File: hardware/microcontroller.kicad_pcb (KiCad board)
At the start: 2 copper layers, 50.8 x 78.7 mm, 44 parts, among them J5 1x2 jumper right-angle, J6 Conn_02x03_Odd_Even, J7 1x2 jumper right-angle, U10 74HC670, U11 74HC670, U13 74AHC74, U15 74LVC138, U16 74LV1T125, U17 74LVC138, U18 74LVC2G125, U3 74LV163, U4 74LV163, U5 74LV163, U6 74LV163, U7 74LV163, U8 74LV164, U9 74LV164

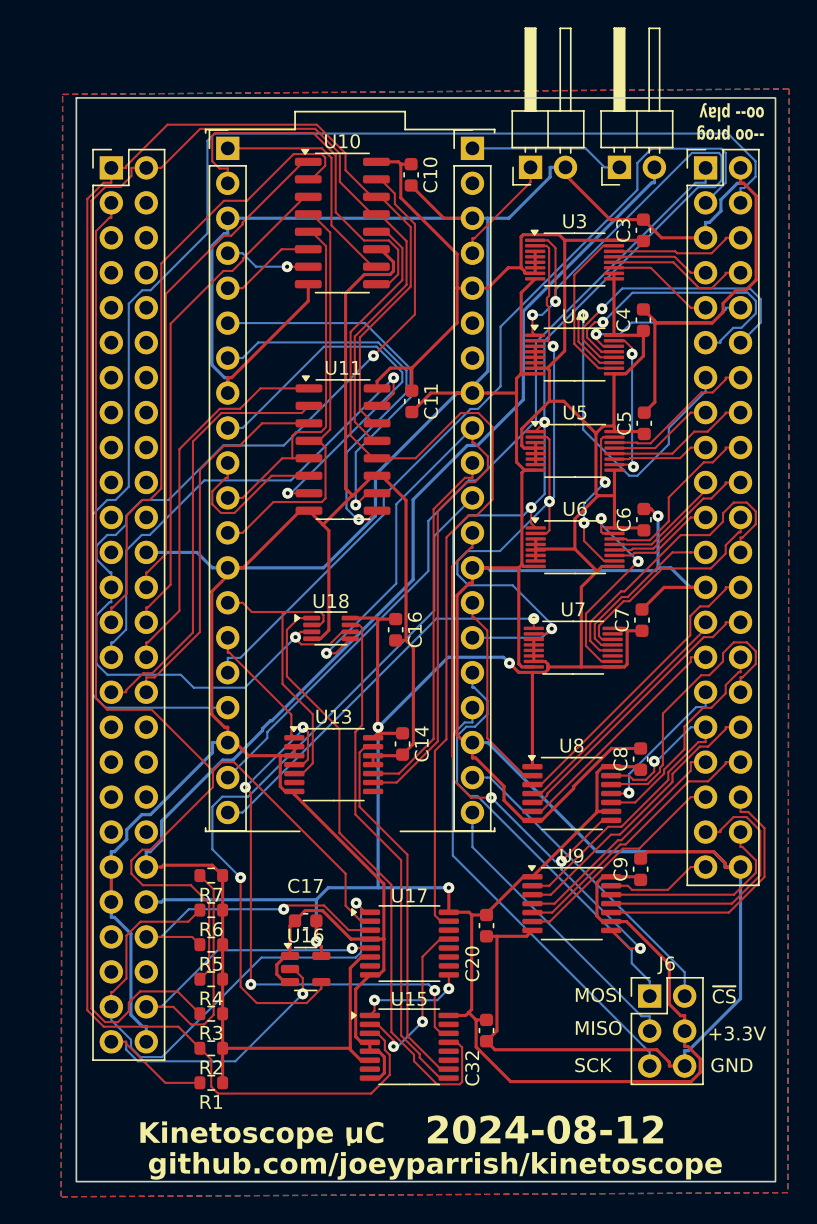
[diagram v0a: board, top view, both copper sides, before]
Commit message: Replace address counters with slightly larger versions that can be assembled more easily
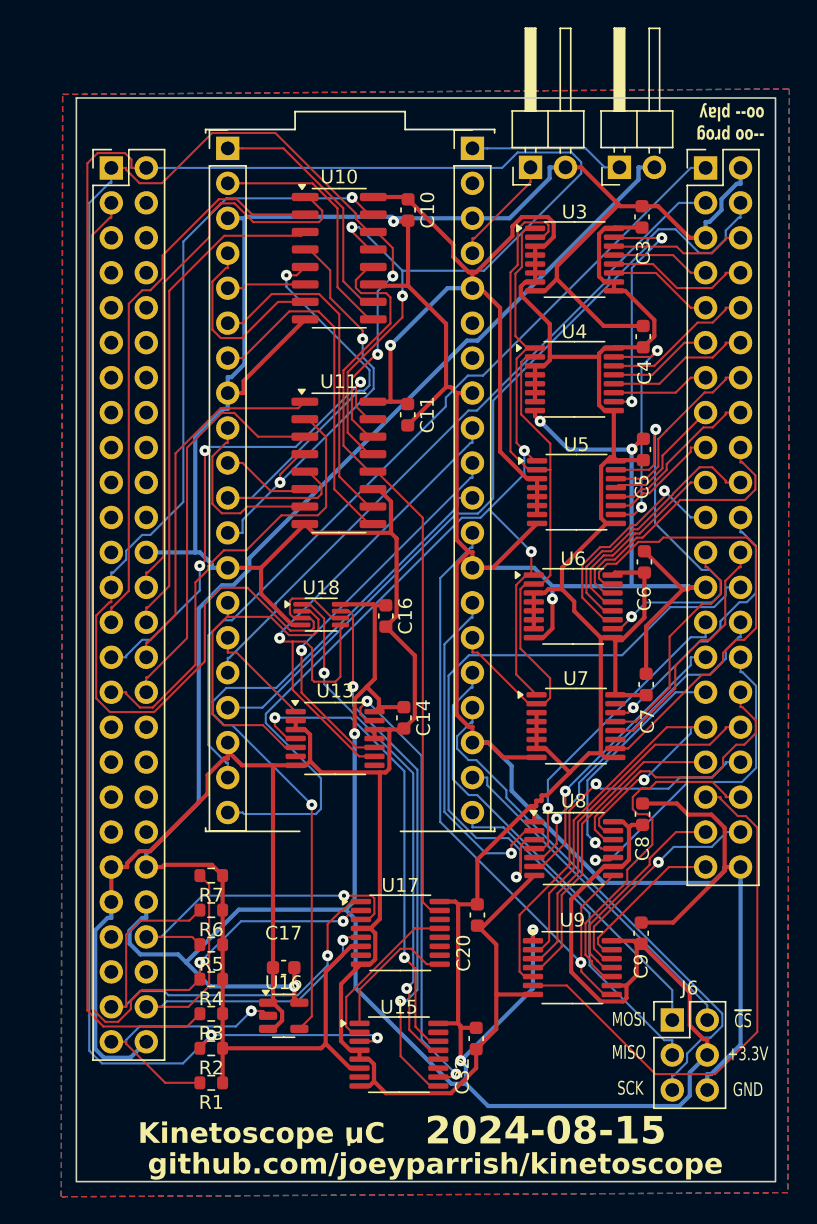
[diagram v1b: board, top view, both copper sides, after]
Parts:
- U3, U4, U5, U6, U7: footprint Package_SO:TSSOP-16_4.4x3.6mm_P0.4mm -> Package_SO:TSSOP-16_4.4x5mm_P0.65mm
- moved U7 5.70 mm to (55.0, 64.9)
- moved C7 4.68 mm to (60.1, 61.9)
- moved C9 4.65 mm to (59.8, 80.0)
- moved U9 4.65 mm to (54.8, 82.5)
- moved U6 4.30 mm to (54.8, 56.2)
- moved C8 4.00 mm to (59.9, 71.3)
- moved U8 4.00 mm to (54.9, 73.8)
- moved C17 3.76 mm to (33.8, 82.5)
- moved U16 3.76 mm to (33.8, 86.0)
- moved C6 3.07 mm to (60.0, 53.0)
- moved U5 3.00 mm to (55.1, 47.9)
- moved C10 2.56 mm to (42.8, 27.4)
- moved U10 2.56 mm to (37.8, 30.9)
- moved J6 2.39 mm to (62.0, 86.3)
- moved C14 1.90 mm to (42.5, 64.3)
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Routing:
- net +3.3V: track 286.7 -> 341.7 mm, vias 4 -> 5
- net /SRAM_DIS_2: track 99.2 -> 59.3 mm
- net GND: track 487.9 -> 451.8 mm, vias 1 -> 4
- net /kinetoscope-header-internal/SEGA_A2: track 115.8 -> 148.4 mm, vias 0 -> 2
- net /data-register-internal/D0: track 22.0 -> 46.1 mm, vias 0 -> 1
- net /data-register-internal/D11: track 16.3 -> 39.8 mm
- net /~{SRAM_W_A_CLR}: track 102.5 -> 79.3 mm, vias 5 -> 2
- net /address-counter-internal/A8: track 28.1 -> 7.12 mm, vias 1 -> 0
- net Net-(U6-TC): track 16.3 -> 34.5 mm, vias 2 -> 0
- net Net-(U5-TC): track 12.0 -> 28.8 mm
- net /REG_R_D6: track 29.8 -> 13.3 mm, vias 1 -> 0
- net /~{REG_WE}: track 69.1 -> 54.6 mm
- net /address-counter-internal/A6: track 22.1 -> 7.64 mm, vias 1 -> 0
- net /SRAM_DIS_1: track 61.4 -> 50.1 mm
- net /address-counter-internal/A7: track 21.9 -> 10.5 mm, vias 1 -> 0
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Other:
- board text added: "2024-08-15"
- board text removed: "2024-08-12"

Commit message: Fix microcontroller address decoders
Verified on a breadboard
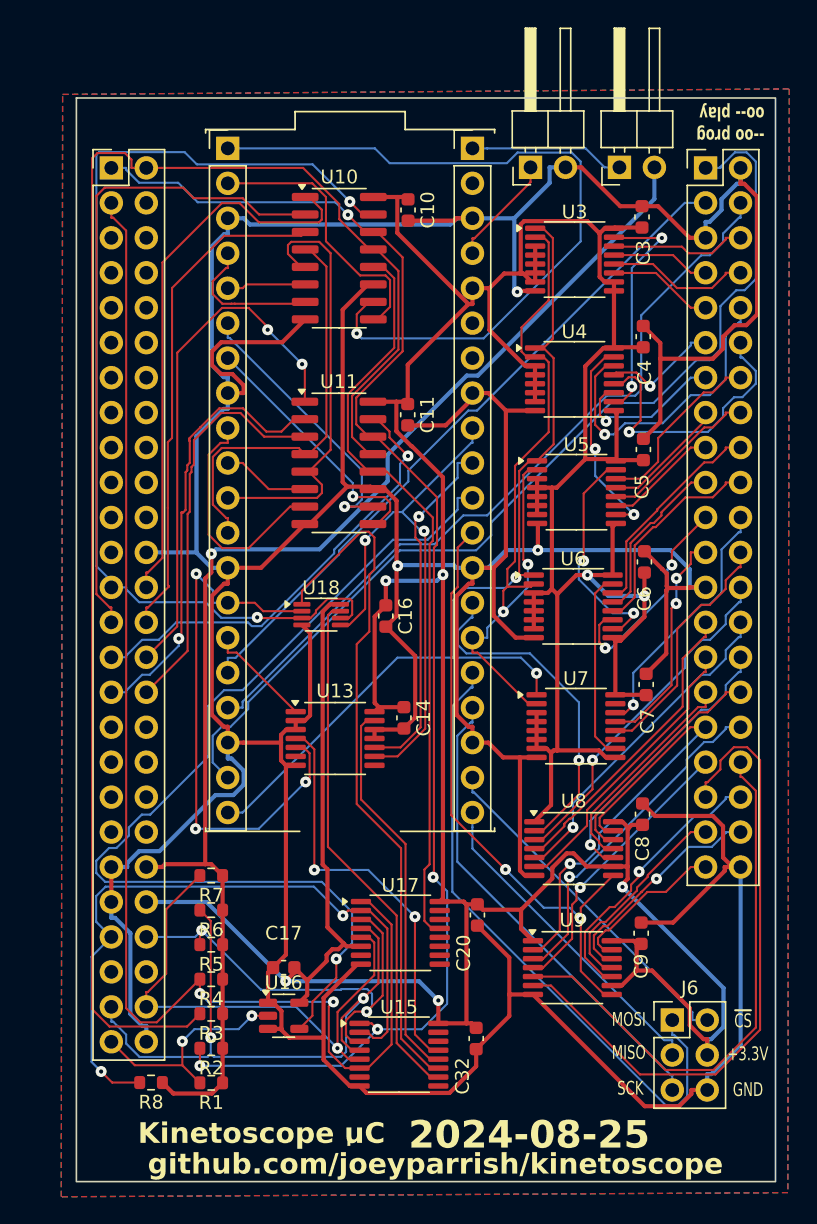
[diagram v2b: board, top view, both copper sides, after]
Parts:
- added R8: 10k, Resistor_SMD:R_0603_1608Metric, F.Cu at (24.2, 90.8)
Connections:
- net /address-counter-internal/A1 renamed /SRAM_W_A0
- net /address-counter-internal/A10 renamed /SRAM_W_A9
- net /address-counter-internal/A11 renamed /SRAM_W_A10
- net /address-counter-internal/A12 renamed /SRAM_W_A11
- net /address-counter-internal/A13 renamed /SRAM_W_A12
- net /address-counter-internal/A14 renamed /SRAM_W_A13
- net /address-counter-internal/A15 renamed /SRAM_W_A14
- net /address-counter-internal/A16 renamed /SRAM_W_A15
- net /address-counter-internal/A17 renamed /SRAM_W_A16
- net /address-counter-internal/A18 renamed /SRAM_W_A17
- net /address-counter-internal/A19 renamed /SRAM_W_A18
- net /address-counter-internal/A2 renamed /SRAM_W_A1
- net /address-counter-internal/A3 renamed /SRAM_W_A2
- net /address-counter-internal/A4 renamed /SRAM_W_A3
- net /address-counter-internal/A5 renamed /SRAM_W_A4
- net /address-counter-internal/A6 renamed /SRAM_W_A5
- net /address-counter-internal/A7 renamed /SRAM_W_A6
- net /address-counter-internal/A8 renamed /SRAM_W_A7
- net /address-counter-internal/A9 renamed /SRAM_W_A8
- net /data-register-internal/D0 renamed /SRAM_D_IN0
- net /data-register-internal/D1 renamed /SRAM_D_IN1
- net /data-register-internal/D10 renamed /SRAM_D_IN10
- net /data-register-internal/D11 renamed /SRAM_D_IN11
- net /data-register-internal/D12 renamed /SRAM_D_IN12
- net /data-register-internal/D13 renamed /SRAM_D_IN13
- net /data-register-internal/D14 renamed /SRAM_D_IN14
- net /data-register-internal/D15 renamed /SRAM_D_IN15
- net /data-register-internal/D2 renamed /SRAM_D_IN2
- net /data-register-internal/D3 renamed /SRAM_D_IN3
- net /data-register-internal/D4 renamed /SRAM_D_IN4
- net /data-register-internal/D5 renamed /SRAM_D_IN5
- net /data-register-internal/D6 renamed /SRAM_D_IN6
- net /data-register-internal/D7 renamed /SRAM_D_IN7
- net /data-register-internal/D8 renamed /SRAM_D_IN8
- net /data-register-internal/D9 renamed /SRAM_D_IN9
- J1 pad 45: /kinetoscope-header-internal/~{SEGA_OE} -> /~{SEGA_OE}
- U15 pad 1: /~{SYNC_OE} -> /kinetoscope-header-internal/SEGA_A1
- U15 pad 10: /~{ERR_CLR} -> /~{ERR_OE}
- U15 pad 11: unconnected-(U15-~{Y4}-Pad11) -> /~{CMD_OE}
- U15 pad 12: unconnected-(U15-~{Y3}-Pad12) -> /~{ERR_CLR}
- U15 pad 13: /~{CMD_OE} -> /~{CMD_SET}
- U15 pad 14: /~{CMD_SET} -> unconnected-(U15-~{Y1}-Pad14)
- U15 pad 2: /~{SYNC_WE} -> /~{SEGA_OE}
- U15 pad 3: /kinetoscope-header-internal/SEGA_A1 -> /~{SEGA_WE_LB}
- U15 pad 4: GND -> /~{SEGA_REGISTER}
- U15 pad 5: GND -> /~{SEGA_AS}
- U15 pad 6: +5V -> /kinetoscope-header-internal/SEGA_A3
- U15 pad 9: /~{ERR_OE} -> unconnected-(U15-~{Y6}-Pad9)
- U17 pad 1: /~{SEGA_REGISTER} -> /kinetoscope-header-internal/SEGA_A3
- U17 pad 13: /~{SYNC_WE} -> /~{REG_WE}
- U17 pad 15: /~{REG_WE} -> unconnected-(U17-~{Y0}-Pad15)
- U17 pad 2: /kinetoscope-header-internal/SEGA_A3 -> /~{SEGA_OE}
- U17 pad 4: GND -> /~{SEGA_REGISTER}
- U17 pad 6: +5V -> +3.3V
- U17 pad 9: /~{SYNC_OE} -> unconnected-(U17-~{Y6}-Pad9)
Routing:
- net /~{SEGA_OE}: track 0.00 -> 50.1 mm, vias 0 -> 2
- net /REG_R_D0: track 18.3 -> 54.8 mm, vias 0 -> 1
- net /kinetoscope-header-internal/SEGA_A2: track 148.4 -> 113.0 mm, vias 2 -> 0
- net /kinetoscope-header-internal/SEGA_A1: track 131.8 -> 105.5 mm
- net /SRAM_D_IN0: track 46.1 -> 25.3 mm
- net Net-(U6-TC): track 34.5 -> 13.8 mm
- net /~{RESET_3V}: track 52.9 -> 72.0 mm
- net /CMD_3V: track 25.1 -> 40.7 mm, vias 0 -> 3
- net /kinetoscope-header-internal/SEGA_A3: track 83.6 -> 98.3 mm
- net /SPI_MOSI: track 32.9 -> 46.4 mm
- net +5V: track 108.3 -> 95.1 mm, vias 0 -> 1
- net /~{CMD_OE}: track 37.6 -> 50.1 mm, vias 2 -> 0
- net Net-(U5-TC): track 28.8 -> 16.6 mm
- net /~{SYNC_WE}: track 12.1 -> 0.00 mm
- net /SRAM_D_IN10: track 28.6 -> 40.1 mm, vias 1 -> 0
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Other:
- board text added: "2024-08-25"
- board text removed: "2024-08-15"

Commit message: Simplify microcontroller board BOM
Replace 74LV1T125 with 74LVC2G125, which simplifies the BOM by removing one special part.
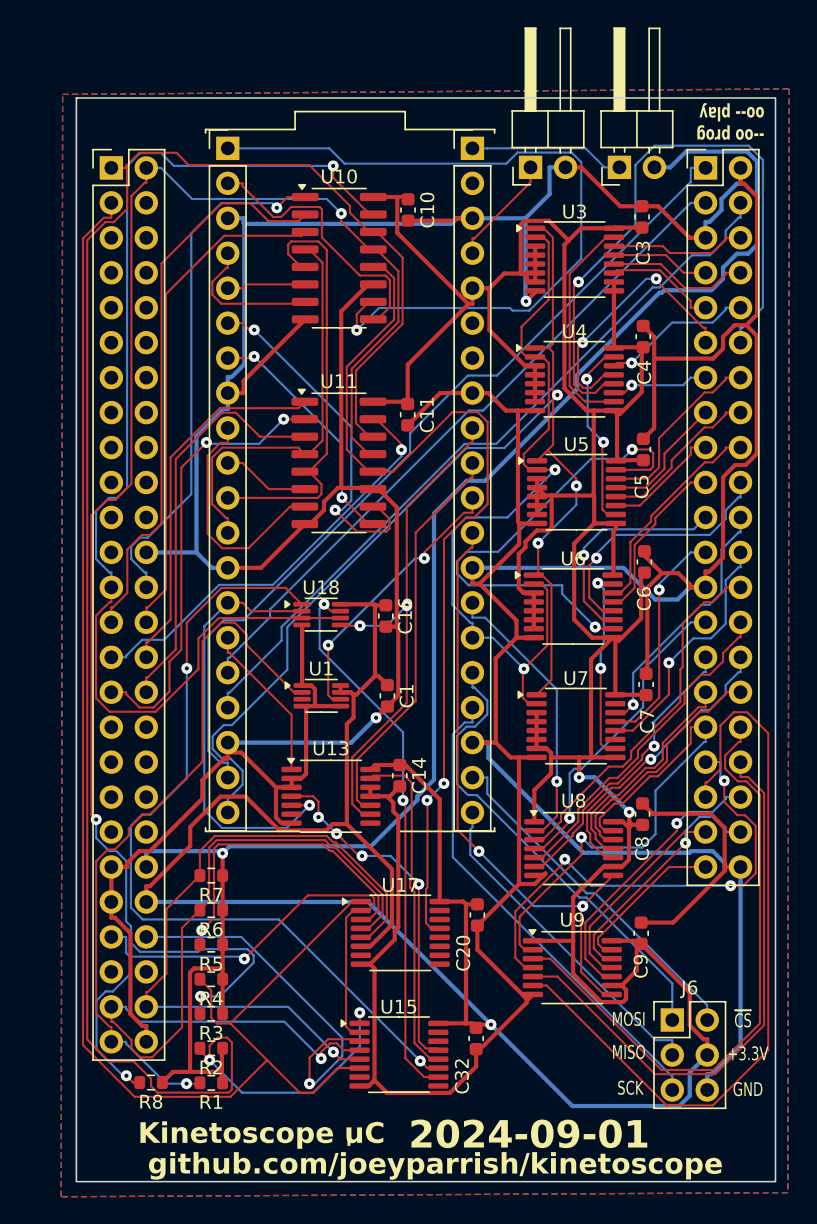
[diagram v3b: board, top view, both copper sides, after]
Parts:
- removed C17: 22nF, Capacitor_SMD:C_0603_1608Metric
- removed U16: 74LV1T125, Package_TO_SOT_SMD:SOT-23-5
- added C1: 22nF, Capacitor_SMD:C_0603_1608Metric, F.Cu at (41.3, 62.7)
- added U1: 74LVC2G125, Package_SO:VSSOP-8_2.3x2mm_P0.5mm, F.Cu at (36.5, 62.7)
- moved C14 4.21 mm to (42.2, 68.5)
- moved U13 4.21 mm to (37.2, 70.0)
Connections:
- net Net-(U3-TC) renamed /address-counter-internal/AR0
- net Net-(U4-TC) renamed /address-counter-internal/AR1
- net Net-(U5-TC) renamed /address-counter-internal/AR2
- net Net-(U6-TC) renamed /address-counter-internal/AR3
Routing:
- net /~{RESET_3V}: track 72.0 -> 20.4 mm, vias 1 -> 2
- net /kinetoscope-header-internal/SEGA_A1: track 105.5 -> 141.8 mm, vias 4 -> 2
- net /~{SEGA_RESET}: track 16.4 -> 51.6 mm, vias 2 -> 1
- net /SRAM_W_A6: track 20.8 -> 45.5 mm
- net +5V: track 95.1 -> 119.3 mm
- net /SRAM_D_IN8: track 24.8 -> 44.7 mm, vias 1 -> 0
- net /address-counter-internal/AR2: track 16.6 -> 35.8 mm
- net /~{SEGA_WE_LB}: track 33.3 -> 52.0 mm
- net /~{SRAM_W_A_CLR}: track 68.5 -> 85.4 mm, vias 2 -> 3
- net /SRAM_D_IN9: track 20.6 -> 35.8 mm, vias 1 -> 3
- net /~{SEGA_REGISTER}: track 46.9 -> 61.0 mm, vias 2 -> 1
- net /~{REG_WE}: track 54.9 -> 68.5 mm, vias 0 -> 2
- net /SPI_MOSI: track 46.4 -> 34.2 mm
- net /~{SEGA_AS}: track 38.2 -> 50.1 mm
- net /SEGA_D5: track 38.1 -> 26.7 mm, vias 2 -> 0
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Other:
- board text added: "2024-09-01"
- board text removed: "2024-08-25"

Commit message: Tweak part numbers
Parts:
- U15, U17: value 74LVC138 -> 74LVC138A
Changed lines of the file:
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@@
 			)
 		)
-		(property "Value" "74LVC138"
+		(property "Value" "74LVC138A"
 			(at 0 3.45 0)
 			(layer "F.Fab")
@@
 			)
 		)
-		(property "Value" "74LVC138"
+		(property "Value" "74LVC138A"
 			(at 0 3.45 0)
 			(layer "F.Fab")
